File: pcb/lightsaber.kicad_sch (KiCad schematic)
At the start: 52 parts, among them J1 2012670005, J2 ESP32 Prog, J3 ESP32 JTAG, J4 Screw_Terminal_01x05, Q1 PMOS, SW1 SW_Push, SW2 SW_Push, U1 ME6211A33PG-N, U2 ESP32-S3-WROOM-1, U3 BQ21040DBVR, U4 MAX17048G+T10, U5 AHT20

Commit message: Adding multiverse
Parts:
- added C21: 1uF, Capacitor_SMD:C_0402_1005Metric, symbol Device:C_Small
- added D5: 1N4148, Diode_SMD:D_SOD-323, symbol Diode:1N4148
- added J5: Conn_01x02, symbol Connector_Generic:Conn_01x02
- added Q2: NPN, Package_TO_SOT_SMD:SOT-23, symbol Simulation_SPICE:NPN
- added R11: 1k, Resistor_SMD:R_0603_1608Metric, symbol Device:R_Small
- added R12: 10k, Resistor_SMD:R_0603_1608Metric, symbol Device:R_Small
- added R13: 10R, Resistor_SMD:R_0402_1005Metric, symbol Device:R_Small
- added U6: 5994, CityTheatrical:Module 5994, symbol CityTheatrical:City_Theatrical_Module
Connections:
- net +3.3V: now also C21.2, R13.2, U6.2 (VCC), U6.3 (VCC)
- net CTI_I2C_nATTN: now also U2.11 (GPIO18/U1RXD/ADC2_CH7/CLK_OUT3), U6.16 (I2C_nATTN)
- net CTI_SPI_CLK: now also U2.20 (GPIO12/TOUCH12/ADC2_CH1/FSPICLK/FSPIIO6/SUBSPICLK), U6.21 (SPI_CLK)
- net CTI_SPI_MISO: now also U2.21 (GPIO13/TOUCH13/ADC2_CH2/FSPIQ/FSPIIO7/SUBSPIQ), U6.20 (SPI_MISO)
- net CTI_SPI_MOSI: now also U2.19 (GPIO11/TOUCH11/ADC2_CH0/FSPID/FSPIIO5/SUBSPID), U6.19 (SPI_MOSI)
- net CTI_SPI_nATTN: now also U2.22 (GPIO14/TOUCH14/ADC2_CH3/FSPIWP/FSPIDQS/SUBSPIWP), U6.22 (SPI_nATTN)
- net CTI_SPI_nSS: now also U2.18 (GPIO10/TOUCH10/ADC1_CH9/FSPICS0/FSPIIO4/SUBSPICS0), U6.18 (SPI_nSS)
- net CTI_nRESET: now also U2.10 (GPIO17/U1TXD/ADC2_CH6), U6.7 (nRESET)
- net ESP32_I2C_SCL: now also U6.14 (I2C_SCL)
- net ESP32_I2C_SDA: now also U6.15 (I2C_SDA)
- net GND: now also C21.1, Q2.3 (E), R12.1, U6.1 (GND), U6.12 (GND), U6.13 (GND), U6.17 (GND), U6.23 (GND), U6.24 (GND), U6.4 (GND), U6.8 (GND)
- new net: Q2.2 (B), R11.2, R12.2
- new net: D5.1 (K), J5.1 (Pin_1), R13.1
- new net: D5.2 (A), J5.2 (Pin_2), Q2.1 (C)
- new net CTI_TCK: U6.6 (JTAG_TCK)
- new net CTI_TMS: U6.5 (JTAG_TMS)
- new net ESP_MOTOR: R11.1
- no-connect marks 21 -> 24
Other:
- note added: "City Theatrical Module"
- note added: "LED Driver"
- note added: "Motor Controller"

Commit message: Initial routing
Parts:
- removed JP1, JP2: SolderJumper_2_Open, Jumper:SolderJumper-2_P1.3mm_Open_Pad1.0x1.5mm, symbol Jumper:SolderJumper_2_Open
- C20, U5: now not fitted; now left out of the parts list
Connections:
- net +3V3 is gone; now on net +3.3V: C20.1, U5.2 (VDD)
- net D+: now also U2.14 (GPIO20/U1CTS/ADC2_CH9/CLK_OUT1/USB_D+)
- net D-: now also U2.13 (GPIO19/U1RTS/ADC2_CH8/CLK_OUT2/USB_D-)
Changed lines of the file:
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@@
     (stroke (width 0) (type default))
   )
-  (wire (pts (xy 513.08 54.61) (xy 518.16 54.61))
-    (stroke (width 0) (type default))
-  )
   (wire (pts (xy 513.08 92.71) (xy 528.32 92.71))
     (stroke (width 0) (type default))
@@
     (stroke (width 0) (type default))
   )
-  (wire (pts (xy 513.08 52.07) (xy 518.16 52.07))
+  (wire (pts (xy 513.08 52.07) (xy 528.32 52.07))
     (stroke (width 0) (type default))
   )
@@
     (stroke (width 0) (type default))
   )
-  (wire (pts (xy 525.78 54.61) (xy 528.32 54.61))
+  (wire (pts (xy 513.08 54.61) (xy 528.32 54.61))
     (stroke (width 0) (type default))
   )
@@
     (stroke (width 0) (type default))
   )
-  (wire (pts (xy 525.78 52.07) (xy 528.32 52.07))
-    (stroke (width 0) (type default))
-  )
   (wire (pts (xy 388.62 238.76) (xy 388.62 243.84))
     (stroke (width 0) (type default))
@@
   )
   (symbol (lib_id "Device:C_Small") (at 205.74 260.35 0) (unit 1)
-    (in_bom yes) (on_board yes) (dnp no) (fields_autoplaced)
+    (in_bom no) (on_board no) (dnp yes) (fields_autoplaced)
     (property "Reference" "C20" (at 208.28 259.7213 0)
       (effects (font (size 1.27 1.27)) (justify left))
@@
       (effects (font (size 1.27 1.27)) hide)
     )
-    (pin "1")
-    (pin "2")
-    (instances
-      (project "lightsaber"
-        (path "/480b6f8b-587f-4642-8a87-aec0c171ba44"
-          (reference "C20") (unit 1)
-        )
-      )
-      (project "CTI_ESP32"
-        (path "/6d3948e0-7215-4b5f-a564-64550d12cd9d"
-          (reference "C3") (unit 1)
-        )
-      )
-    )
-  )
-  (symbol (lib_id "Jumper:SolderJumper_2_Open") (at 521.97 52.07 0) (unit 1)
-    (in_bom yes) (on_board yes) (dnp no) (fields_autoplaced)
-    (property "Reference" "JP1" (at 521.97 46.99 0)
-      (effects (font (size 1.27 1.27)))
-    )
-    (property "Value" "SolderJumper_2_Open" (at 521.97 49.53 0)
-      (effects (font (size 1.27 1.27)))
-    )
-    (property "Footprint" "Jumper:SolderJumper-2_P1.3mm_Open_Pad1.0x1.5mm" (at 521.97 52.07 0)
-      (effects (font (size 1.27 1.27)) hide)
-    )
-    (property "Datasheet" "~" (at 521.97 52.07 0)
+    (property "Sim.Enable" "0" (at 205.74 260.35 0)
       (effects (font (size 1.27 1.27)) hide)
     )
@@
       (project "lightsaber"
         (path "/480b6f8b-587f-4642-8a87-aec0c171ba44"
-          (reference "JP1") (unit 1)
+          (reference "C20") (unit 1)
         )
       )
       (project "CTI_ESP32"
         (path "/6d3948e0-7215-4b5f-a564-64550d12cd9d"
-          (reference "JP1") (unit 1)
+          (reference "C3") (unit 1)
         )
       )
@@
     )
   )
-  (symbol (lib_id "Jumper:SolderJumper_2_Open") (at 521.97 54.61 0) (unit 1)
-    (in_bom yes) (on_board yes) (dnp no)
-    (property "Reference" "JP2" (at 521.97 49.53 0)
-      (effects (font (size 1.27 1.27)))
-    )
-    (property "Value" "SolderJumper_2_Open" (at 521.97 57.15 0)
-      (effects (font (size 1.27 1.27)))
-    )
-    (property "Footprint" "Jumper:SolderJumper-2_P1.3mm_Open_Pad1.0x1.5mm" (at 521.97 54.61 0)
-      (effects (font (size 1.27 1.27)) hide)
-    )
-    (property "Datasheet" "~" (at 521.97 54.61 0)
-      (effects (font (size 1.27 1.27)) hide)
-    )
-    (pin "1")
-    (pin "2")
-    (instances
-      (project "lightsaber"
-        (path "/480b6f8b-587f-4642-8a87-aec0c171ba44"
-          (reference "JP2") (unit 1)
-        )
-      )
-      (project "CTI_ESP32"
-        (path "/6d3948e0-7215-4b5f-a564-64550d12cd9d"
-          (reference "JP2") (unit 1)
-        )
-      )
-    )
-  )
   (symbol (lib_id "Device:R_Small") (at 205.74 57.15 0) (unit 1)
     (in_bom yes) (on_board yes) (dnp no) (fields_autoplaced)
@@
     )
   )
-  (symbol (lib_id "power:+3V3") (at 205.74 248.92 0) (unit 1)
-    (in_bom yes) (on_board yes) (dnp no) (fields_autoplaced)
-    (property "Reference" "#PWR031" (at 205.74 252.73 0)
-      (effects (font (size 1.27 1.27)) hide)
-    )
-    (property "Value" "+3V3" (at 205.74 243.84 0)
-      (effects (font (size 1.27 1.27)))
-    )
-    (property "Footprint" "" (at 205.74 248.92 0)
-      (effects (font (size 1.27 1.27)) hide)
-    )
-    (property "Datasheet" "" (at 205.74 248.92 0)
-      (effects (font (size 1.27 1.27)) hide)
-    )
-    (pin "1")
-    (instances
-      (project "lightsaber"
-        (path "/480b6f8b-587f-4642-8a87-aec0c171ba44"
-          (reference "#PWR031") (unit 1)
-        )
-      )
-    )
-  )
   (symbol (lib_id "Device:C_Small") (at 143.51 153.67 0) (unit 1)
     (in_bom yes) (on_board yes) (dnp no) (fields_autoplaced)
@@
     )
   )
+  (symbol (lib_id "power:+3.3V") (at 205.74 248.92 0) (unit 1)
+    (in_bom yes) (on_board yes) (dnp no) (fields_autoplaced)
+    (property "Reference" "#PWR031" (at 205.74 252.73 0)
+      (effects (font (size 1.27 1.27)) hide)
+    )
+    (property "Value" "+3.3V" (at 205.74 245.11 0)
+      (effects (font (size 1.27 1.27)))
+    )
+    (property "Footprint" "" (at 205.74 248.92 0)
+      (effects (font (size 1.27 1.27)) hide)
+    )
+    (property "Datasheet" "" (at 205.74 248.92 0)
+      (effects (font (size 1.27 1.27)) hide)
+    )
+    (pin "1")
+    (instances
+      (project "lightsaber"
+        (path "/480b6f8b-587f-4642-8a87-aec0c171ba44"
+          (reference "#PWR031") (unit 1)
+        )
+      )
+      (project "CTI_ESP32"
+        (path "/6d3948e0-7215-4b5f-a564-64550d12cd9d"
+          (reference "#PWR036") (unit 1)
+        )
+      )
+    )
+  )
   (symbol (lib_id "power:+BATT") (at 40.64 96.52 0) (unit 1)
     (in_bom yes) (on_board yes) (dnp no) (fields_autoplaced)
@@
   )
   (symbol (lib_id "AHT20:AHT20") (at 186.69 260.35 0) (unit 1)
-    (in_bom yes) (on_board yes) (dnp no) (fields_autoplaced)
+    (in_bom no) (on_board no) (dnp yes) (fields_autoplaced)
     (property "Reference" "U5" (at 186.69 247.65 0)
       (effects (font (size 1.27 1.27)))
@@
       (effects (font (size 1.27 1.27)) hide)
     )
+    (property "Sim.Enable" "0" (at 186.69 260.35 0)
+      (effects (font (size 1.27 1.27)) hide)
+    )

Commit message: Fuses and current detection
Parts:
- added C22, C23, C24: 100nF, Capacitor_SMD:C_0402_1005Metric, symbol Device:C_Small
- added D6: WS2812B, LED_SMD:LED_WS2812B_PLCC4_5.0x5.0mm_P3.2mm, symbol LED:WS2812B
- added F1: 8A Fuse, Littelfuse:0154008DR, symbol Littelfuse:0154008.DR
- added IC1: BMI055, BMI:QFN50P300X450X100-16N, symbol BMI:BMI055
- added U7: ACS725xLCTR-10AU, Package_SO:SOIC-8_3.9x4.9mm_P1.27mm, symbol Sensor_Current:ACS725xLCTR-10AU
- J4: footprint Connector_PinHeader_1.27mm:PinHeader_1x05_P1.27mm_Horizontal -> TerminalBlock_Phoenix:TerminalBlock_Phoenix_MPT-0,5-5-2.54_1x05_P2.54mm_Horizontal
- J5: footprint (none) -> Connector_JST:JST_XH_S2B-XH-A-1_1x02_P2.50mm_Horizontal
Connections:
- net +3.3V: now also C22.1, C23.1, C24.1, D6.1 (VDD), IC1.11 (VDDIO), IC1.3 (VDD), IC1.7 (PS), U7.8 (VCC)
- net +BATT: now also F1.1, U7.1 (IP+), U7.2 (IP+); no longer C11.1 (VBAT), J4.1 (Pin_1)
- net ESP32_I2C_SCL: now also IC1.8 (SCX)
- net ESP32_I2C_SDA: now also IC1.9 (SDX)
- net GND: now also C22.2, C23.2, C24.2, D6.3 (VSS), IC1.10 (SDO2), IC1.15 (SDO1), IC1.4 (GNDA), IC1.6 (GNDIO), U7.5 (GND)
- net at D4.2 (DOUT): now also D6.4 (DIN)
- new net: C11.1 (VBAT), F1.2
- new net ESP32_BMI_ACCEL_1: IC1.12 (INT3)
- new net ESP32_BMI_ACCEL_2: IC1.13 (INT4)
- new net ESP32_BMI_GYRO_1: IC1.16 (INT1)
- new net ESP32_BMI_GYRO_2: IC1.1 (INT2)
- new net ESP_CURRENT_SENSE: U7.7 (VIOUT)
- new net LED_PWR: J4.1 (Pin_1), U7.3 (IP-), U7.4 (IP-)
- no-connect marks 24 -> 26
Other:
- note added: "Capacitors?"
- note added: "Check this setup"
- note added: "Find some right angled units"
- note added: "JTAG Header"
- note added: "LED Current monitoring"
- note added: "MPU"
- moved on the sheet: C11

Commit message: General tidyup
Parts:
- removed C7: 10uF, Capacitor_SMD:C_0603_1608Metric, symbol Device:C_Small
- added C25: 1nF, Capacitor_SMD:C_0402_1005Metric, symbol Device:C_Small
- IC1: LCSC (none) -> C189620
- U3: footprint BQ21040DBVR:SOT95P280X145-6N -> BQ21040:SOT95P280X145-6N
- U4: footprint MAX17048G_T10:SON50P200X200X80-9N -> MAX17048:SON50P200X200X80-9N
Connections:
- net ESP32_BMI_ACCEL_1: now also U2.6 (GPIO6/TOUCH6/ADC1_CH5)
- net ESP32_BMI_ACCEL_2: now also U2.7 (GPIO7/TOUCH7/ADC1_CH6)
- net ESP32_BMI_GYRO_1: now also U2.4 (GPIO4/TOUCH4/ADC1_CH3)
- net ESP32_BMI_GYRO_2: now also U2.5 (GPIO5/TOUCH5/ADC1_CH4)
- net ESP_CURRENT_SENSE: now also U2.15 (GPIO3/TOUCH3/ADC1_CH2)
- net GND: now also C25.2
- net at U7.6 (FILTER): now also C25.1
- no-connect marks 26 -> 27
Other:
- note added: "Do we want a full disconnect for LEDs when we're on battery power?"
- note added: "Used as a switch to disconnect battery power when USB source available."
- note removed: "Used as a switch to disconnecty battery power when USB source available."
- moved on the sheet: C24, Q1, R4

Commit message: Pre-review
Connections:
- net ESP_MOTOR: now also U2.23 (GPIO21)
- no-connect marks 27 -> 26
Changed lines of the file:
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@@
   (no_connect (at 36.83 49.53))
   (no_connect (at 265.43 320.04))
-  (no_connect (at 513.08 102.87))
   (no_connect (at 513.08 64.77))
   (no_connect (at 109.22 196.85))
@@
     (stroke (width 0) (type default))
   )
+  (wire (pts (xy 513.08 102.87) (xy 528.32 102.87))
+    (stroke (width 0) (type default))
+  )
   (wire (pts (xy 416.56 52.07) (xy 421.64 52.07))
     (stroke (width 0) (type default))
@@
   )
   (text "Battery Holder" (at 34.29 87.63 0)
-    (effects (font (size 3 3) bold (color 0 255 0 1)) (justify left bottom))
+    (effects (font (size 3 3) bold (color 255 0 0 1)) (justify left bottom))
   )
   (text "Position as far away from \nbattery charging as possible"
@@
   )
   (text "USB-C Connector" (at 36.83 22.86 0)
-    (effects (font (size 3 3) bold (color 0 255 0 1)) (justify left bottom))
+    (effects (font (size 3 3) bold (color 255 0 0 1)) (justify left bottom))
   )
   (text "JTAG Headers" (at 171.45 91.44 0)
-    (effects (font (size 3 3) bold (color 0 0 255 1)) (justify left bottom))
+    (effects (font (size 3 3) bold (color 255 0 0 1)) (justify left bottom))
   )
   (text "Motor Controller" (at 341.63 241.3 0)
-    (effects (font (size 3 3) bold (color 0 0 255 1)) (justify left bottom))
+    (effects (font (size 3 3) bold (color 255 0 0 1)) (justify left bottom))
   )
   (text "Charging\n" (at 115.57 151.13 0)
@@
   )
   (text "I2C Pull up" (at 231.14 149.86 0)
-    (effects (font (size 3 3) bold (color 0 0 255 1)) (justify left bottom))
+    (effects (font (size 3 3) bold (color 255 0 0 1)) (justify left bottom))
   )
   (text "LED Driver" (at 331.47 147.32 0)
-    (effects (font (size 3 3) bold (color 0 0 255 1)) (justify left bottom))
+    (effects (font (size 3 3) bold (color 255 0 0 1)) (justify left bottom))
   )
   (text "Reset Buttons" (at 168.91 149.86 0)
-    (effects (font (size 3 3) bold (color 0 0 255 1)) (justify left bottom))
+    (effects (font (size 3 3) bold (color 255 0 0 1)) (justify left bottom))
   )
   (text "Battery Fuel Gauge" (at 33.02 184.15 0)
-    (effects (font (size 3 3) (thickness 0.6) bold (color 0 0 255 1)) (justify left bottom))
+    (effects (font (size 3 3) (thickness 0.6) bold (color 255 0 0 1)) (justify left bottom))
   )
   (text "Tooling hole" (at 170.18 199.39 0)
-    (effects (font (size 3 3) (thickness 0.6) bold) (justify left bottom))
+    (effects (font (size 3 3) (thickness 0.6) bold (color 255 0 0 1)) (justify left bottom))
   )
   (text "Find some right angled units" (at 359.41 156.21 0)
@@
   )
   (text "Battery Disconnect" (at 161.29 20.32 0)
-    (effects (font (size 3 3) bold (color 0 255 0 1)) (justify left bottom))
+    (effects (font (size 3 3) bold (color 255 0 0 1)) (justify left bottom))
   )
   (text "Do we want a full disconnect for LEDs when we're\non battery power?"
@@
   )
   (text "Pheonix Connector" (at 36.83 242.57 0)
-    (effects (font (size 3 3) bold (color 0 0 255 1)) (justify left bottom))
+    (effects (font (size 3 3) bold (color 255 0 0 1)) (justify left bottom))
   )
   (text "ESD Protection" (at 101.6 48.26 0)
     (effects (font (size 1.27 1.27) (color 0 0 255 1)) (justify left bottom))
   )
-  (text "Check connection numbers" (at 229.87 119.38 0)
+  (text "Check connection numbers" (at 229.87 120.65 0)
     (effects (font (size 1.27 1.27) (color 255 0 0 1)) (justify left bottom))
   )
   (text "LED Current monitoring" (at 24.13 294.64 0)
-    (effects (font (size 3 3) bold (color 0 0 255 1)) (justify left bottom))
+    (effects (font (size 3 3) bold (color 255 0 0 1)) (justify left bottom))
   )
   (text "Check this setup" (at 361.95 251.46 0)
@@
   )
   (text "Battery Charger" (at 34.29 127 0)
-    (effects (font (size 3 3) bold (color 0 0 255 1)) (justify left bottom))
+    (effects (font (size 3 3) bold (color 255 0 0 1)) (justify left bottom))
   )
   (text "JTAG Header" (at 461.01 185.42 0)
@@
   )
   (text "MPU" (at 261.62 284.48 0)
-    (effects (font (size 3 3) bold (color 0 0 255 1)) (justify left bottom))
+    (effects (font (size 3 3) bold (color 255 0 0 1)) (justify left bottom))
   )
   (text "Humidity and Temp\nsensor" (at 156.21 241.3 0)
-    (effects (font (size 2 2) (thickness 0.4) bold) (justify left bottom))
+    (effects (font (size 2 2) (thickness 0.4) bold (color 255 0 0 1)) (justify left bottom))
   )
   (text "Check connection numbers" (at 175.26 120.65 0)
@@
   )
   (text "ESP32 Module" (at 430.53 24.13 0)
-    (effects (font (size 3 3) (thickness 0.6) bold (color 0 0 255 1)) (justify left bottom))
+    (effects (font (size 3 3) (thickness 0.6) bold (color 255 0 0 1)) (justify left bottom))
   )
   (text "10%" (at 21.59 40.64 0)
@@
   )
   (text "City Theatrical Module" (at 453.39 162.56 0)
-    (effects (font (size 3 3) bold (color 0 0 255 1)) (justify left bottom))
+    (effects (font (size 3 3) bold (color 255 0 0 1)) (justify left bottom))
   )
   (text "3.3V Regulator" (at 238.76 20.32 0)
-    (effects (font (size 3 3) bold (color 0 255 0 1)) (justify left bottom))
+    (effects (font (size 3 3) bold (color 255 0 0 1)) (justify left bottom))
   )
   (label "CHG_LED" (at 118.11 147.32 0) (fields_autoplaced)

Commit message: ERC Complete
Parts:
- removed C10, C19: 1uF, Capacitor_SMD:C_0402_1005Metric, symbol Device:C_Small
- removed D6: WS2812B, LED_SMD:LED_WS2812B_PLCC4_5.0x5.0mm_P3.2mm, symbol LED:WS2812B
- removed H1, H2, H3: Tooling Hole, AHT20:MountingHole_1.152mm, symbol Mechanical:MountingHole
- removed R1: 10k, Resistor_SMD:R_0603_1608Metric, symbol Device:R_Small
- added C17: 4.7nF, Capacitor_SMD:C_0402_1005Metric, symbol Device:C_Small
- added C21, C22: 1uF, Capacitor_SMD:C_0402_1005Metric, symbol Device:C_Small
- added D6: LED, LED_SMD:LED_0603_1608Metric, symbol Device:LED
- added JP1: 10k Bridge, Jumper:SolderJumper-3_P1.3mm_Bridged12_Pad1.0x1.5mm, symbol Jumper:SolderJumper_3_Bridged12
- added R12, R13: 10k, Resistor_SMD:R_0603_1608Metric, symbol Device:R_Small
- D3: LCSC C72043 -> C84256
- J5: footprint Connector_JST:JST_XH_S2B-XH-A-1_1x02_P2.50mm_Horizontal -> Connector_PinHeader_2.54mm:PinHeader_1x02_P2.54mm_Horizontal
- U3: renamed from U7; now left out of the parts list
- renumbered C22 to C10, C23 to C11, C25 to C16, C21 to C18, C11 to C19, C18 to C20, C17 to C23, C16 to C24, C20 to C25, C8 to C7, C9 to C8, C24 to C9, J4 to J2, J2 to J3, J3 to J4, R2 to R1, R9 to R10, R13 to R11, R12 to R14, R3 to R2, R4 to R3, R6 to R4, R7 to R6, R10 to R7, R11 to R8, R8 to R9, SW2 to SW1, SW1 to SW2, U3 to U4, U6 to U5, U4 to U6, U5 to U7
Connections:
- net +3.3V: now also R10.1, R9.1, C22.2, R12.1, R13.1; no longer R10.2, R9.2
- net +BATT: now also U3.3 (IP-), U3.4 (IP-); no longer R5.1, U3.1 (IP+), U3.2 (IP+)
- net ESP32_I2C_SCL: now also R9.2; no longer R10.1
- net ESP32_I2C_SDA: now also R10.2; no longer R9.1
- net ESP_CURRENT_SENSE: now also U2.38 (GPIO2/TOUCH2/ADC1_CH1), C17.1; no longer U2.15 (GPIO3/TOUCH3/ADC1_CH2)
- net ESP_EN: now also R12.2
- net ESP_IO0: now also C24.2, R13.2; no longer C24.1
- net ESP_USER_BUTTON: now also C21.2
- net GND: now also C24.1, C17.2, C21.1, C22.1, JP1.1 (A); no longer C24.2
- net LED_PWR: now also U3.1 (IP+), U3.2 (IP+); no longer U3.3 (IP-), U3.4 (IP-)
- net VDD: now also JP1.3 (B)
- net CTI_TCK: no longer names the net of U5.6 (JTAG_TCK)
- net CTI_TMS: no longer names the net of U5.5 (JTAG_TMS)
- new net: JP1.2 (C), R5.1
- no-connect marks 26 -> 28
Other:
- note added: "0x43 0x38 0x18 0x68"
- note added: "City Theatrical Module Humidty and Temp Sensor Accelerometer Gyroscope"
- note added: "Cut out underneath on PCB"
- note added: "Decive Address: 0x18, 0x68"
- note added: "Decive Address: 0x43"
- note added: "Potential to move"
- note added: "Red"
- note removed: "Capacitors?"
- note removed: "Check connection numbers"
- note removed: "Check this setup"
- note removed: "Do we want a full disconnect for LEDs when we're on battery power?"
- note removed: "Find some right angled units"
- note removed: "JTAG Header"
- note removed: "Tooling hole"
- moved on the sheet: C10, C11, C12, C13, C14, C15, C16, C18, C19, C20, C23, C24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

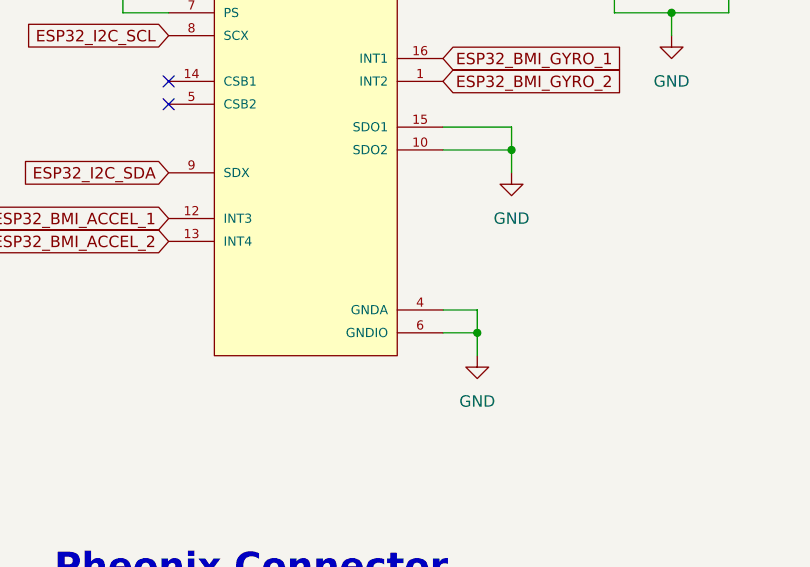
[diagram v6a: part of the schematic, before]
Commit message: All symbols imported
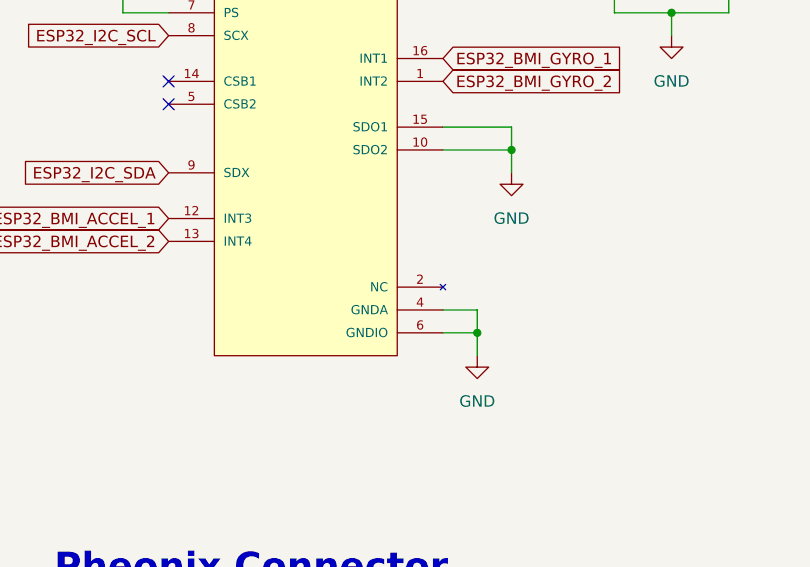
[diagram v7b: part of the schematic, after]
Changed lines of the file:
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@@
     (pin "10")
     (pin "11")
+    (pin "2")
     (pin "12")
     (pin "13")

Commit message: Completed design
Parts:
- added J6: Conn_01x06, Connector_PinHeader_2.54mm:PinHeader_1x06_P2.54mm_Vertical, symbol Connector_Generic:Conn_01x06
- C18, U5: now not fitted; now left out of the parts list
- J1: LCSC C565324 -> C134092
- J5: footprint Connector_PinHeader_2.54mm:PinHeader_1x02_P2.54mm_Horizontal -> TerminalBlock_Phoenix:TerminalBlock_Phoenix_MPT-0,5-2-2.54_1x02_P2.54mm_Horizontal
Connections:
- net +3.3V: no longer R11.2
- net +BATT: now also R11.2
- net CHG_LED: now also D3.1 (K), U4.3 (~{CHG}); no longer D3.2 (A), R4.2
- net ESP32_BMI_ACCEL_2: now also U2.4 (GPIO4/TOUCH4/ADC1_CH3); no longer U2.7 (GPIO7/TOUCH7/ADC1_CH6)
- net ESP32_BMI_GYRO_1: now also U2.5 (GPIO5/TOUCH5/ADC1_CH4); no longer U2.4 (GPIO4/TOUCH4/ADC1_CH3)
- net ESP32_BMI_GYRO_2: now also U2.7 (GPIO7/TOUCH7/ADC1_CH6); no longer U2.5 (GPIO5/TOUCH5/ADC1_CH4)
- net ESP_LED_DATA: now also J2.4 (Pin_4); no longer J2.2 (Pin_2)
- net ESP_USER_BUTTON: now also J2.2 (Pin_2); no longer J2.4 (Pin_4)
- net GND: now also J2.1 (Pin_1); no longer J2.5 (Pin_5)
- net LED_PWR: now also J2.5 (Pin_5); no longer J2.1 (Pin_1)
- net BQ_TS_JUMP: now reaches JP1.2 (C), R5.1
- net MOTOR_TRANSISTOR: now reaches Q2.2 (B), R14.2, R8.2
- net MOTOR_POS: now reaches D5.1 (K), R11.1
- net MOTOR_POS: now also J5.2 (Pin_1); no longer J5.1 (Pin_1)
- net BAT_FUSE: now reaches C19.1 (VBAT), F1.2
- net ACS_FILTER: now reaches C16.1, U3.6 (FILTER)
- net BQ_TS: now reaches R5.2, U4.1 (TS)
- net BQ_ISET: now reaches R6.1, U4.4 (ISET)
- net MOTOR_NEG: now reaches D5.2 (A), Q2.1 (C)
- net MOTOR_NEG: now also J5.1 (Pin_2); no longer J5.2 (Pin_2)
- new net CHG_LED_RES: D3.2 (A), R4.2
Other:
- moved on the sheet: J2
